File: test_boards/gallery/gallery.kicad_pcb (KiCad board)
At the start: 2 copper layers, 33 parts

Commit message: narrowing drills on barrell back footprints
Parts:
- moved CON*** 4.62 mm to (50.2, 148.6)
- moved CON*** 2.84 mm to (31.8, 148.6)
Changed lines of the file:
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@@
     (links 0)
     (no_connects 0)
-    (area 17.030999 11.953599 401.217201 279.357448)
+    (area 16.5354 11.953599 401.217201 279.357448)
     (thickness 1.6)
     (drawings 12)
@@
     (mod_text_size 1 1)
     (mod_text_width 0.15)
-    (pad_size 2.2479 1.4986)
-    (pad_drill 0.8128)
+    (pad_size 4.064 4.064)
+    (pad_drill 2.7432)
     (pad_to_mask_clearance 0)
     (aux_axis_origin 0 0)
@@
     )
   )
-  (module BARREL_JACK_21x55 (layer F.Cu)
-    (at 34.29 149.86)
-    (descr "DC Barrel Jack, 2.1x5.5mm")
-    (tags "Power Jack")
-    (path PWR-Jack)
-    (fp_text reference CON*** (at -7.62 5.461) (layer F.SilkS)
-      (effects (font (size 0.762 0.762) (thickness 0.1524)))
-    )
-    (fp_text value BARREL_JACK (at -4.445 -5.334) (layer F.SilkS) hide
-      (effects (font (size 1.016 1.016) (thickness 0.2032)))
-    )
-    (fp_text user 2.1x5.5mm (at -2.667 -3.556) (layer F.SilkS)
-      (effects (font (size 0.762 0.762) (thickness 0.1524)))
-    )
-    (fp_line (start -10.1981 -4.50088) (end -10.1981 4.50088) (layer F.SilkS) (width 0.381))
-    (fp_line (start -13.69822 -4.50088) (end -13.69822 4.50088) (layer F.SilkS) (width 0.381))
-    (fp_line (start -13.69822 4.50088) (end 0.80264 4.50088) (layer F.SilkS) (width 0.381))
-    (fp_line (start 0.80264 4.50088) (end 0.80264 -4.50088) (layer F.SilkS) (width 0.381))
-    (fp_line (start 0.80264 -4.50088) (end -13.69822 -4.50088) (layer F.SilkS) (width 0.381))
-    (pad 1 thru_hole rect (at 0 0) (size 4.064 4.064) (drill 3.048)
-      (layers *.Cu *.Mask F.SilkS)
-    )
-    (pad 2 thru_hole circle (at -5.969 0) (size 4.064 4.064) (drill 3.048)
-      (layers *.Cu *.Mask F.SilkS)
-    )
-    (pad 3 thru_hole circle (at -3.048 4.699) (size 4.064 4.064) (drill 3.048)
-      (layers *.Cu *.Mask F.SilkS)
-    )
-  )
   (module hole_M3 (layer F.Cu)
     (at 326.39 30.48)
@@
     (fp_circle (center 0 0) (end 4.5 0) (layer F.SilkS) (width 0.15))
     (pad 1 thru_hole circle (at 0 0) (size 6 6) (drill 3.2)
-      (layers *.Cu *.Mask F.SilkS)
-    )
-  )
-  (module BARREL_JACK_25x55 (layer F.Cu)
-    (at 54.61 149.86)
-    (descr "DC Barrel Jack, 2.5x5.5mm")
-    (tags "Power Jack")
-    (path PWR-Jack)
-    (fp_text reference CON*** (at -7.62 5.461) (layer F.SilkS)
-      (effects (font (size 0.762 0.762) (thickness 0.1524)))
-    )
-    (fp_text value BARREL_JACK (at -4.445 -5.334) (layer F.SilkS) hide
-      (effects (font (size 1.016 1.016) (thickness 0.2032)))
-    )
-    (fp_text user 2.5x5.5mm (at -2.667 -3.556) (layer F.SilkS)
-      (effects (font (size 0.762 0.762) (thickness 0.1524)))
-    )
-    (fp_line (start -10.1981 -4.50088) (end -10.1981 4.50088) (layer F.SilkS) (width 0.381))
-    (fp_line (start -13.69822 -4.50088) (end -13.69822 4.50088) (layer F.SilkS) (width 0.381))
-    (fp_line (start -13.69822 4.50088) (end 0.80264 4.50088) (layer F.SilkS) (width 0.381))
-    (fp_line (start 0.80264 4.50088) (end 0.80264 -4.50088) (layer F.SilkS) (width 0.381))
-    (fp_line (start 0.80264 -4.50088) (end -13.69822 -4.50088) (layer F.SilkS) (width 0.381))
-    (pad 1 thru_hole rect (at 0 0) (size 4.064 4.064) (drill 3.048)
-      (layers *.Cu *.Mask F.SilkS)
-    )
-    (pad 2 thru_hole circle (at -5.969 0) (size 4.064 4.064) (drill 3.048)
-      (layers *.Cu *.Mask F.SilkS)
-    )
-    (pad 3 thru_hole circle (at -3.048 4.699) (size 4.064 4.064) (drill 3.048)
       (layers *.Cu *.Mask F.SilkS)
     )
@@
       (layers *.Cu *.Mask F.SilkS)
     )
+  )
+  (module BARREL_JACK_21x55 (layer F.Cu)
+    (at 31.75 148.59)
+    (descr "DC Barrel Jack, 2.1x5.5mm")
+    (tags "Power Jack")
+    (path PWR-Jack)
+    (fp_text reference CON*** (at -7.62 5.461) (layer F.SilkS)
+      (effects (font (size 0.762 0.762) (thickness 0.1524)))
+    )
+    (fp_text value BARREL_JACK (at -4.445 -5.334) (layer F.SilkS) hide
+      (effects (font (size 1.016 1.016) (thickness 0.2032)))
+    )
+    (fp_text user 2.1x5.5mm (at -2.667 -3.556) (layer F.SilkS)
+      (effects (font (size 0.762 0.762) (thickness 0.1524)))
+    )
+    (fp_line (start -10.1981 -4.50088) (end -10.1981 4.50088) (layer F.SilkS) (width 0.254))
+    (fp_line (start -13.69822 -4.50088) (end -13.69822 4.50088) (layer F.SilkS) (width 0.254))
+    (fp_line (start -13.69822 4.50088) (end 0.80264 4.50088) (layer F.SilkS) (width 0.254))
+    (fp_line (start 0.80264 4.50088) (end 0.80264 -4.50088) (layer F.SilkS) (width 0.254))
+    (fp_line (start 0.80264 -4.50088) (end -13.69822 -4.50088) (layer F.SilkS) (width 0.254))
+    (pad 1 thru_hole rect (at 0 0) (size 4.064 4.064) (drill 2.7432)
+      (layers *.Cu *.Mask F.SilkS)
+    )
+    (pad 2 thru_hole circle (at -5.969 0) (size 4.064 4.064) (drill 2.7432)
+      (layers *.Cu *.Mask F.SilkS)
+    )
+    (pad 3 thru_hole circle (at -3.048 4.699) (size 4.064 4.064) (drill 2.7432)
+      (layers *.Cu *.Mask F.SilkS)
+    )
+  )
+  (module BARREL_JACK_25x55 (layer F.Cu)
+    (at 50.165 148.59)
+    (descr "DC Barrel Jack, 2.5x5.5mm")
+    (tags "Power Jack")
+    (path PWR-Jack)
+    (fp_text reference CON*** (at -7.62 5.461) (layer F.SilkS)
+      (effects (font (size 0.762 0.762) (thickness 0.1524)))
+    )
+    (fp_text value BARREL_JACK (at -4.445 -5.334) (layer F.SilkS) hide
+      (effects (font (size 1.016 1.016) (thickness 0.2032)))
+    )
+    (fp_text user 2.5x5.5mm (at -2.667 -3.556) (layer F.SilkS)
+      (effects (font (size 0.762 0.762) (thickness 0.1524)))
+    )
+    (fp_line (start -10.1981 -4.50088) (end -10.1981 4.50088) (layer F.SilkS) (width 0.254))
+    (fp_line (start -13.69822 -4.50088) (end -13.69822 4.50088) (layer F.SilkS) (width 0.254))
+    (fp_line (start -13.69822 4.50088) (end 0.80264 4.50088) (layer F.SilkS) (width 0.254))
+    (fp_line (start 0.80264 4.50088) (end 0.80264 -4.50088) (layer F.SilkS) (width 0.254))
+    (fp_line (start 0.80264 -4.50088) (end -13.69822 -4.50088) (layer F.SilkS) (width 0.254))
+    (pad 1 thru_hole rect (at 0 0) (size 4.064 4.064) (drill 2.7432)
+      (layers *.Cu *.Mask F.SilkS)
+    )
+    (pad 2 thru_hole circle (at -5.969 0) (size 4.064 4.064) (drill 2.7432)
+      (layers *.Cu *.Mask F.SilkS)
+    )
+    (pad 3 thru_hole circle (at -3.048 4.699) (size 4.064 4.064) (drill 2.7432)
+      (layers *.Cu *.Mask F.SilkS)
+    )

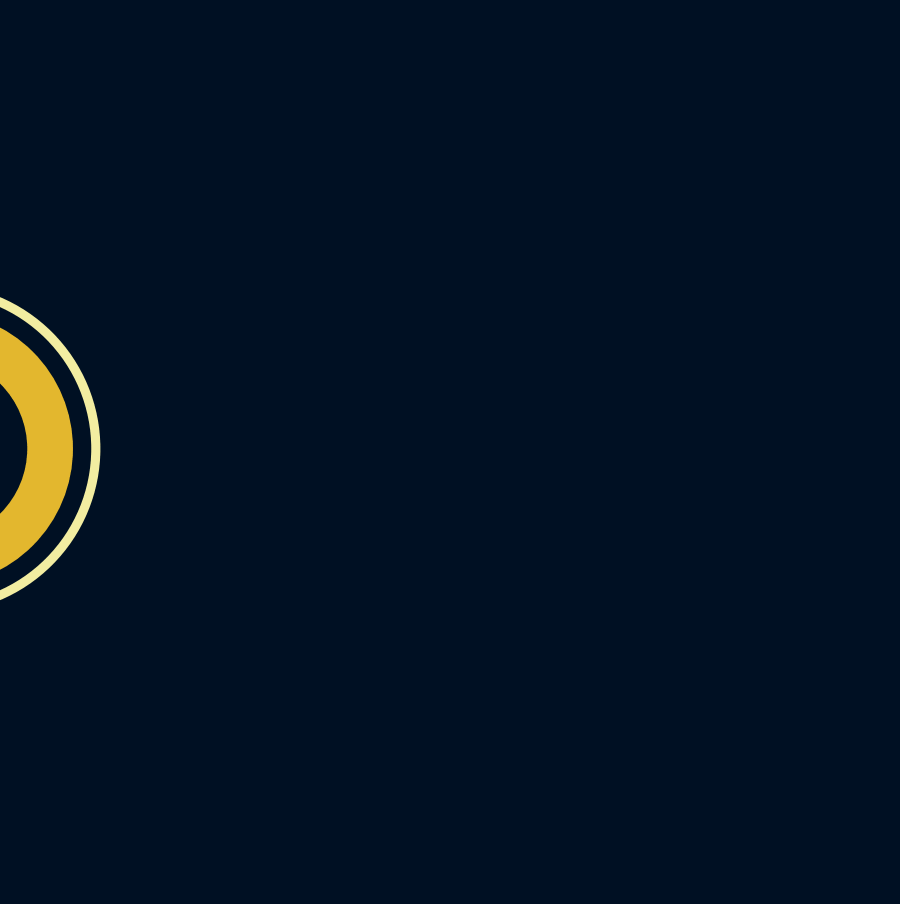
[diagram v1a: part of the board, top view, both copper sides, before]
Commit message: pulling in 4P4C connector and symbol.
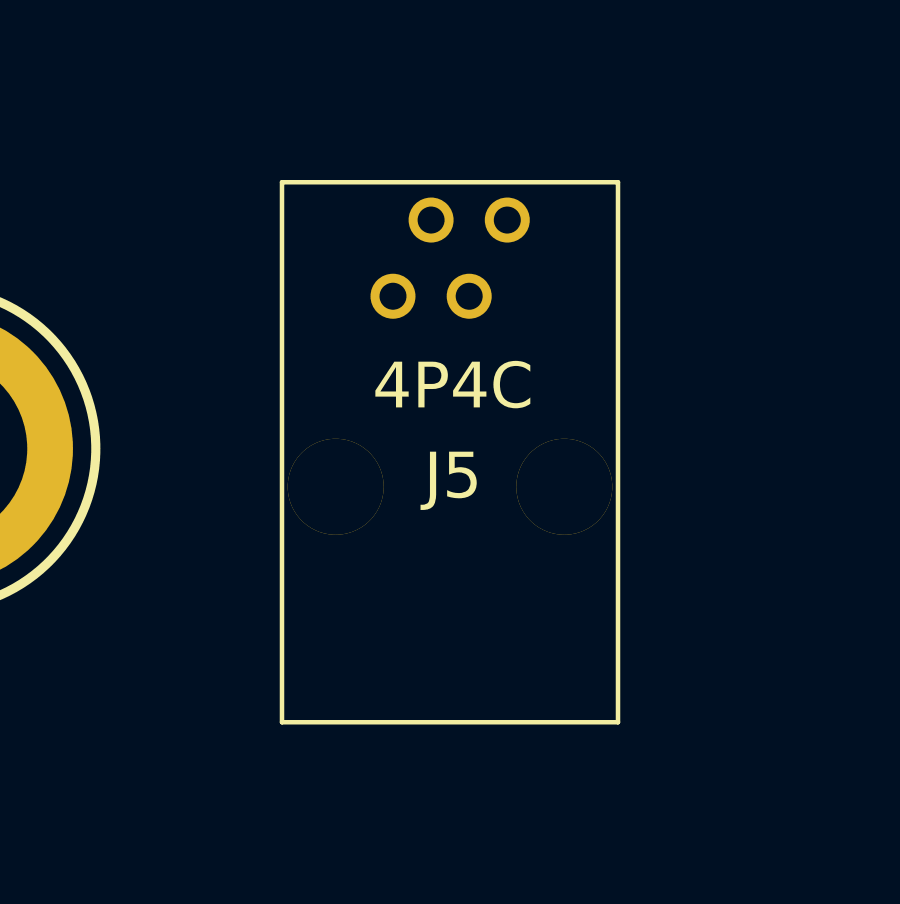
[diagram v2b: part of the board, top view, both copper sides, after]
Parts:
- added J5: 4P4C, A-2004-3-4-LP-N-R, F.Cu at (82.5, 144.8)
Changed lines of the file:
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@@
     (tracks 22)
     (zones 0)
-    (modules 33)
-    (nets 1)
+    (modules 34)
+    (nets 5)
   )
   (page A3)
@@
   )
   (net 0 "")
+  (net 1 N-000001)
+  (net 2 N-000002)
+  (net 3 N-000003)
+  (net 4 N-000004)
   (net_class Default "This is the default net class."
     (clearance 0.254)
@@
     (uvia_drill 0.127)
     (add_net "")
+    (add_net N-000001)
+    (add_net N-000002)
+    (add_net N-000003)
+    (add_net N-000004)
   )
   (module 530002B02500G (layer F.Cu)
@@
       (layers *.Cu *.Mask F.SilkS)
     )
+  )
+  (module A-2004-3-4-LP-N-R (layer F.Cu)
+    (at 82.55 144.78)
+    (fp_text reference J5 (at 2 6) (layer F.SilkS)
+      (effects (font (size 1.524 1.524) (thickness 0.3048)))
+    )
+    (fp_text value 4P4C (at 2 3) (layer F.SilkS)
+      (effects (font (size 1.524 1.524) (thickness 0.3048)))
+    )
+    (fp_line (start -3.7 -3.8) (end -3.7 14.2) (layer F.SilkS) (width 0.15))
+    (fp_line (start 7.5 -3.8) (end 7.5 14.2) (layer F.SilkS) (width 0.15))
+    (fp_line (start -3.7 -3.8) (end 7.5 -3.8) (layer F.SilkS) (width 0.15))
+    (fp_line (start -3.7 14.2) (end 7.5 14.2) (layer F.SilkS) (width 0.15))
+    (pad 2 thru_hole circle (at 1.27 -2.54) (size 1.5 1.5) (drill 0.9)
+      (layers *.Cu *.Mask F.SilkS)
+      (net 2 N-000002)
+    )
+    (pad 4 thru_hole circle (at 3.81 -2.54) (size 1.5 1.5) (drill 0.9)
+      (layers *.Cu *.Mask F.SilkS)
+      (net 3 N-000003)
+    )
+    (pad 1 thru_hole circle (at 0 0) (size 1.5 1.5) (drill 0.9)
+      (layers *.Cu *.Mask F.SilkS)
+      (net 4 N-000004)
+    )
+    (pad 3 thru_hole circle (at 2.54 0) (size 1.5 1.5) (drill 0.9)
+      (layers *.Cu *.Mask F.SilkS)
+      (net 1 N-000001)
+    )
+    (pad 6 thru_hole circle (at 5.71 6.35) (size 3.2 3.2) (drill 3.2)
+      (layers *.Cu *.Mask F.SilkS)
+    )
+    (pad 5 thru_hole circle (at -1.91 6.35) (size 3.2 3.2) (drill 3.2)
+      (layers *.Cu *.Mask F.SilkS)
+    )

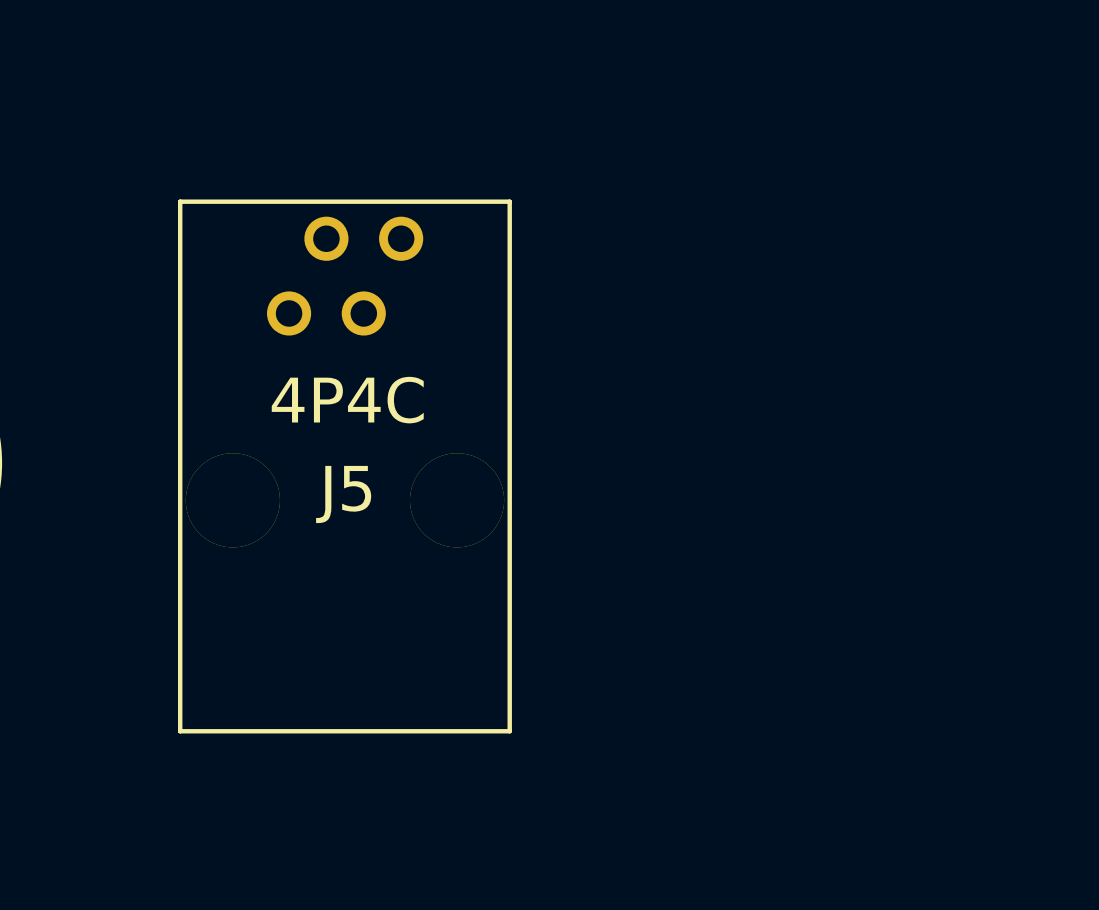
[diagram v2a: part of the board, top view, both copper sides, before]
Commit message: adding additional 4P4C footprint.
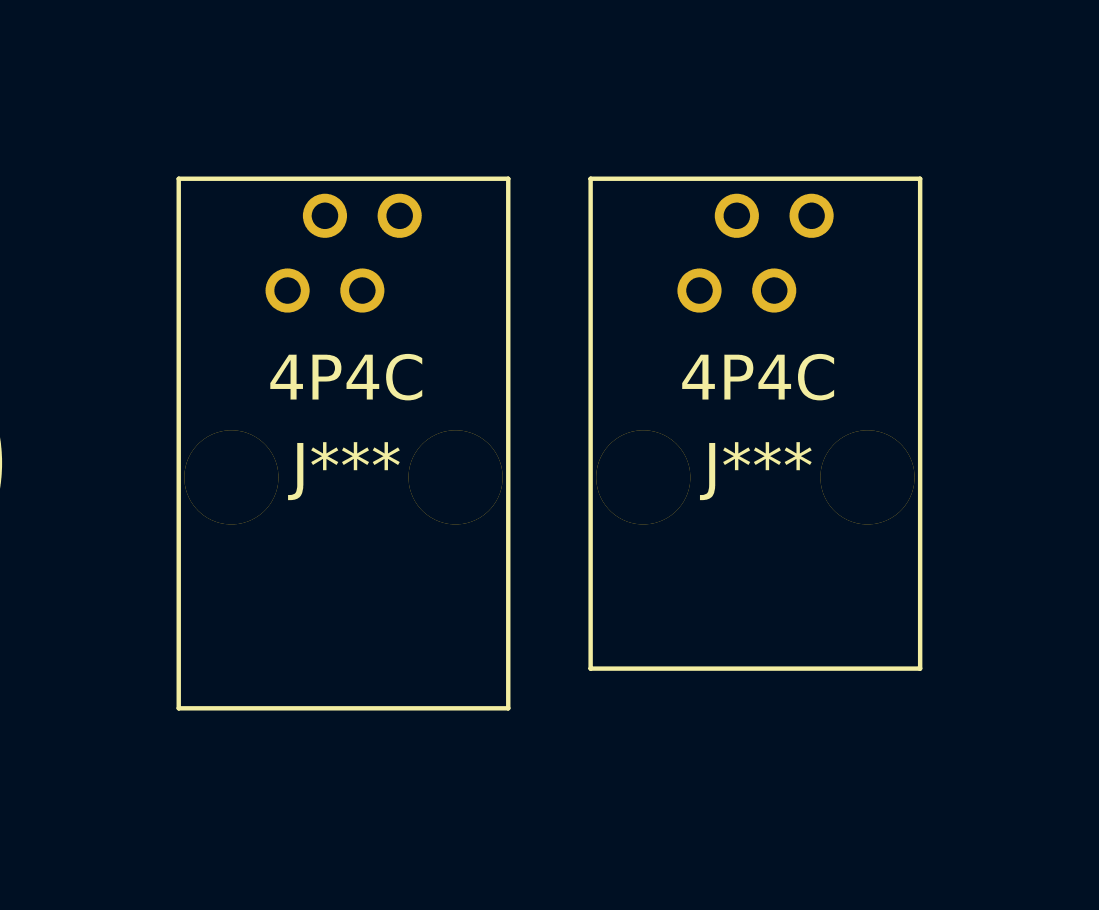
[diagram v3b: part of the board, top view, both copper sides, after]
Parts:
- removed J5: 4P4C, A-2004-3-4-LP-N-R
- added J***: 4P4C, A-2004-3-4-LP-N-R, F.Cu at (82.5, 144.0)
- added J***: 4P4C, A-2014-3-4-N-T-R, F.Cu at (96.5, 144.0)
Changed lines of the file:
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@@
     (tracks 22)
     (zones 0)
-    (modules 34)
-    (nets 5)
+    (modules 35)
+    (nets 1)
   )
   (page A3)
@@
     (mod_text_size 1 1)
     (mod_text_width 0.15)
-    (pad_size 4.064 4.064)
-    (pad_drill 2.7432)
+    (pad_size 1.5 1.5)
+    (pad_drill 0.9)
     (pad_to_mask_clearance 0)
     (aux_axis_origin 0 0)
@@
   )
   (net 0 "")
-  (net 1 N-000001)
-  (net 2 N-000002)
-  (net 3 N-000003)
-  (net 4 N-000004)
   (net_class Default "This is the default net class."
     (clearance 0.254)
@@
     (uvia_drill 0.127)
     (add_net "")
-    (add_net N-000001)
-    (add_net N-000002)
-    (add_net N-000003)
-    (add_net N-000004)
   )
   (module 530002B02500G (layer F.Cu)
@@
   )
   (module A-2004-3-4-LP-N-R (layer F.Cu)
-    (at 82.55 144.78)
-    (fp_text reference J5 (at 2 6) (layer F.SilkS)
+    (at 82.5 144)
+    (fp_text reference J*** (at 2 6) (layer F.SilkS)
       (effects (font (size 1.524 1.524) (thickness 0.3048)))
     )
@@
     (pad 2 thru_hole circle (at 1.27 -2.54) (size 1.5 1.5) (drill 0.9)
       (layers *.Cu *.Mask F.SilkS)
-      (net 2 N-000002)
     )
     (pad 4 thru_hole circle (at 3.81 -2.54) (size 1.5 1.5) (drill 0.9)
       (layers *.Cu *.Mask F.SilkS)
-      (net 3 N-000003)
     )
     (pad 1 thru_hole circle (at 0 0) (size 1.5 1.5) (drill 0.9)
       (layers *.Cu *.Mask F.SilkS)
-      (net 4 N-000004)
     )
     (pad 3 thru_hole circle (at 2.54 0) (size 1.5 1.5) (drill 0.9)
       (layers *.Cu *.Mask F.SilkS)
-      (net 1 N-000001)
     )
     (pad 6 thru_hole circle (at 5.71 6.35) (size 3.2 3.2) (drill 3.2)
+      (layers *.Cu *.Mask F.SilkS)
+    )
+    (pad 5 thru_hole circle (at -1.91 6.35) (size 3.2 3.2) (drill 3.2)
+      (layers *.Cu *.Mask F.SilkS)
+    )
+  )
+  (module A-2014-3-4-N-T-R (layer F.Cu)
+    (at 96.5 144)
+    (fp_text reference J*** (at 2 6) (layer F.SilkS)
+      (effects (font (size 1.524 1.524) (thickness 0.3048)))
+    )
+    (fp_text value 4P4C (at 2 3) (layer F.SilkS)
+      (effects (font (size 1.524 1.524) (thickness 0.3048)))
+    )
+    (fp_line (start -3.7 -3.8) (end -3.7 12.85) (layer F.SilkS) (width 0.15))
+    (fp_line (start 7.5 -3.8) (end 7.5 12.85) (layer F.SilkS) (width 0.15))
+    (fp_line (start -3.7 -3.8) (end 7.5 -3.8) (layer F.SilkS) (width 0.15))
+    (fp_line (start -3.7 12.85) (end 7.5 12.85) (layer F.SilkS) (width 0.15))
+    (pad 2 thru_hole circle (at 1.27 -2.54) (size 1.5 1.5) (drill 0.9)
+      (layers *.Cu *.Mask F.SilkS)
+    )
+    (pad 4 thru_hole circle (at 3.81 -2.54) (size 1.5 1.5) (drill 0.9)
+      (layers *.Cu *.Mask F.SilkS)
+    )
+    (pad 1 thru_hole circle (at 0 0) (size 1.5 1.5) (drill 0.9)
+      (layers *.Cu *.Mask F.SilkS)
+    )
+    (pad 3 thru_hole circle (at 2.54 0) (size 1.5 1.5) (drill 0.9)
+      (layers *.Cu *.Mask F.SilkS)
+    )
+    (pad 6 thru_hole circle (at 5.71 6.35) (size 3.2 3.2) (drill 3.2)
